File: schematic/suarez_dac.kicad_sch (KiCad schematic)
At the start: 26 parts, among them M1 1 / 0.15 um, M10 2 / 0.35 um LVT, M11 1 / 0.15 um, M12 2 / 0.35 um LVT, M13 4 / 2 um, M14 4 / 2 um, M15 4 / 1 um LVT, M16 4 / 1 um LVT, M17 4 / 2 um, M18 4 / 2 um, M19 24 / 2 um, M2 2 / 0.15 um, M20 20 / 1 um, M3 1 / 0.15 um, M4 2 / 0.15 um, M5 1 / 0.15 um, M6 2 / 0.15 um, M7 1 / 0.15 um, M8 2 / 0.35 um LVT, M9 1 / 0.15 um

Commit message: Connect schematic signal path and add illustrated design documentation
Draw reference selection, SAMPLE/HOLD banks, amplifier bias, feedback,
output stage, and compensation as connected circuits. Retain device pin
numbers, models, geometry, and the qualified silicon implementation.

Add schematic, actual-GDS, all-code, mismatch, stability, settling, and
phase-timing figures, plus circuit, testing, and reproduction guides.

Validation: zero KiCad ERC violations; 72 pin connections, all 26 device
property sets, and symbol pin names match design.json. All 87 local
documentation links resolve; evidence audit passes. GDS and RC hashes
remain unchanged. Refresh the release manifest and figure generators.
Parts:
- removed M10, M12, M8: 2 / 0.35 um LVT, symbol Sky130:PMOS_TG3
- removed M11, M7, M9: 1 / 0.15 um, symbol Sky130:NMOS3
- removed M16: 4 / 1 um LVT, symbol Sky130:PMOS3
- removed M17: 4 / 2 um, symbol Sky130:NMOS3
- removed R1, R2: 171 kR nominal, symbol Sky130:R_Small_US
- added M10, M12, M8: 2 / 0.35 um LVT, symbol Sky130:PMOS_H3
- added M11, M7, M9: 1 / 0.15 um, symbol Sky130:NMOS_H3
- added M16: 4 / 1 um LVT, symbol Sky130:PMOS_R3
- added M17: 4 / 2 um, symbol Sky130:NMOS_R3
- added R1, R2: 171 kR, symbol Sky130:R_Small_US_H
- R3: value 80 kR nominal -> 80 kR
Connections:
- net BIAS: now also R1.1
- net HOLD: now also M11.3 (S), M12.3 (S)
- net H_BAR: now also M8.2 (G)
- net L_BAR: now also M10.2 (G)
- net MIRROR: now also M16.1 (D), M17.1 (D), M17.2 (G)
- net RBMID: now also R1.2, R2.1
- net SAMPLE: now also M10.3 (S), M11.1 (D), M12.1 (D), M7.3 (S), M8.3 (S), M9.3 (S)
- net S_BAR: now also M12.2 (G)
- net TAIL: now also M16.3 (S)
- net VGND: now also M17.3 (S), R2.2
- net ua[0]: now also M7.1 (D), M8.1 (D)
- net ua[1]: now also M16.2 (G)
- net ua[2]: now also M10.1 (D), M9.1 (D)
- net ui_in[0]: now also M7.2 (G)
- net ui_in[1]: now also M9.2 (G)
- net ui_in[2]: now also M11.2 (G)
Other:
- note added: "01 REFERENCE SELECTION AND CHARGE SHARING"
- note added: "02 UNITY-GAIN BUFFER / BIAS, FEEDBACK AND COMPENSATION"
- note added: "03 COMPLEMENTARY PHASE DRIVERS"
- note added: "8 bits, LSB first: charge 2 us; dead 0.2 us; share 2 us; dead 0.2 us. Read 3 us after bit 7."
- note added: "Bodies: all NMOS -> VGND; all PMOS -> VDPWR. Body ties are explicit in SPICE / silicon."
- note added: "C1 / C2: 16 MIM units per bank"
- note added: "HIGH"
- note added: "HIGH / LOW never overlap. LOW / SHARE overlap only during initialization. External controller supplies dead time."
- note added: "Initialize: HIGH=0, LOW=1, SHARE=1 for 8 us. Then all phases off for 0.2 us."
- note added: "LOW"
- note added: "OPERATING SEQUENCE"
- note added: "R3-C3 compensation belongs to the buffer"
- note added: "SHARE"
- note added: "SKY130 | 1.8 V | 8 bits, LSB first | 161 x 225.76 um | W / L dimensions in um"
- note added: "SUAREZ SERIAL CHARGE-SHARING DAC"
- note added: "Switches: N 1 / 0.15; P 2 / 0.35 LVT"
- note added: "VOUT"
- note added: "VREFH = 0.9 V"
- note added: "VREFL = 0.2 V"
- note added: "unity-gain feedback"
- note removed: "01 CHARGE REDISTRIBUTION"
- note removed: "02 BUFFER COMPENSATION"
- note removed: "03 COMPLEMENTARY SWITCH CONTROLS"
- note removed: "04 INPUT AMPLIFIER AND BIAS"
- note removed: "05 OUTPUT DRIVER"
- note removed: "16 x (14 / 14 um) MIM"
- note removed: "Buffered analog output"
- note removed: "Bulk ties: every NMOS -> VGND; every PMOS -> VDPWR. Bulk pins are implicit in this drawing and explicit in the silicon netlist."
- note removed: "C1 and C2 perform the D/A conversion."
- note removed: "C3 stabilizes the output buffer."
- note removed: "CHARGE HIGH"
- note removed: "CHARGE LOW"
- note removed: "External phases provide dead time."
- note removed: "HIGH and LOW must never overlap. SHARE closes only after HIGH / LOW have opened."
- note removed: "Initialize: HIGH=0, LOW=1, SHARE=1 for 8 us. Then 8 bits, LSB first: charge 2 us, dead 0.2 us, share 2 us, dead 0.2 us."
- note removed: "No on-chip word counter is required."
- note removed: "PORTS"
- note removed: "R3: xhigh poly, 0.35 / 14 um"
- note removed: "SHARE CHARGE"
- note removed: "SUAREZ TWO-CAPACITOR DAC / SKY130"
- note removed: "Tiny Tapeout 1x2 analog macro | 1.8 V | LSB first | transistor dimensions shown as W / L"
- note removed: "Unused digital outputs are tied to VGND; ua[3:7] are isolated. Supply bypassing is provided by the Tiny Tapeout chip / board."
- note removed: "ui_in[0] = HIGH ui_in[1] = LOW ui_in[2] = SHARE ua[0] = VREFH ua[1] = VOUT ua[2] = VREFL"
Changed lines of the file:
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@@
 (kicad_sch (version 20250114) (generator "eeschema")
-(paper "A3") (title_block (title "Suarez two-capacitor DAC") (rev "0.1") (company "SKY130 / Tiny Tapeout"))
+(paper "A3") (title_block (title "Suarez two-capacitor DAC") (rev "0.2") (company "SKY130 / Tiny Tapeout"))

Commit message: Clean up ground symbols and shared supply rails
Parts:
- removed R1, R2: 171 kR, symbol Sky130:R_Small_US_H
- added R1, R2: 171 kR, symbol Sky130:R_Small_US
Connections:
- net BIAS: now also R1.1
- net RBMID: now also R1.2, R2.1
- net VGND: now also R2.2
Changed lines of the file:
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@@
 (kicad_sch (version 20250114) (generator "eeschema")
-(paper "A3") (title_block (title "Suarez two-capacitor DAC") (rev "0.2") (company "SKY130 / Tiny Tapeout"))
+(paper "A3") (title_block (title "Suarez two-capacitor DAC") (rev "0.3") (company "SKY130 / Tiny Tapeout"))

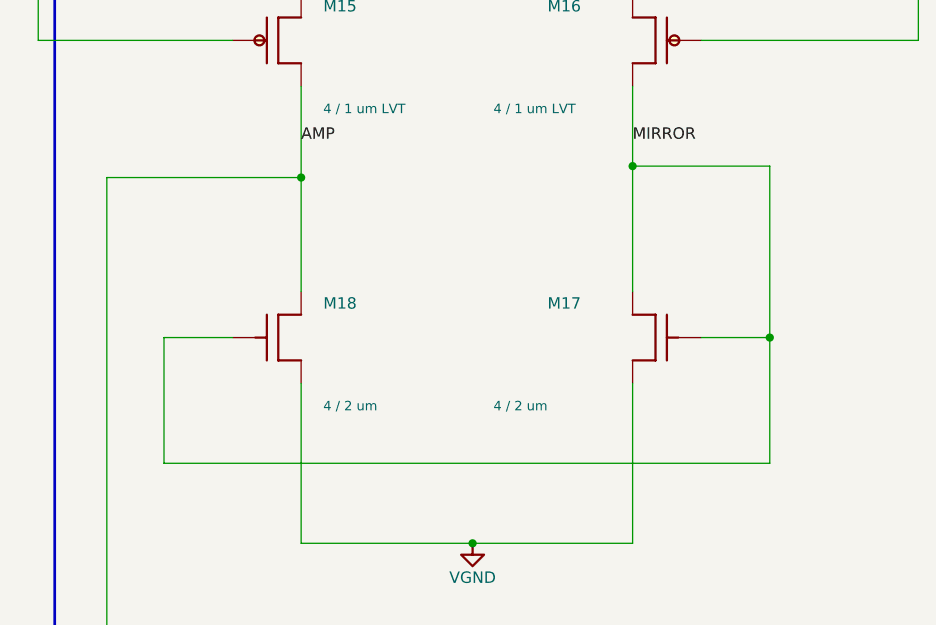
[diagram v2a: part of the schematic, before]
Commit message: Redraw buffer current mirror in conventional schematic form
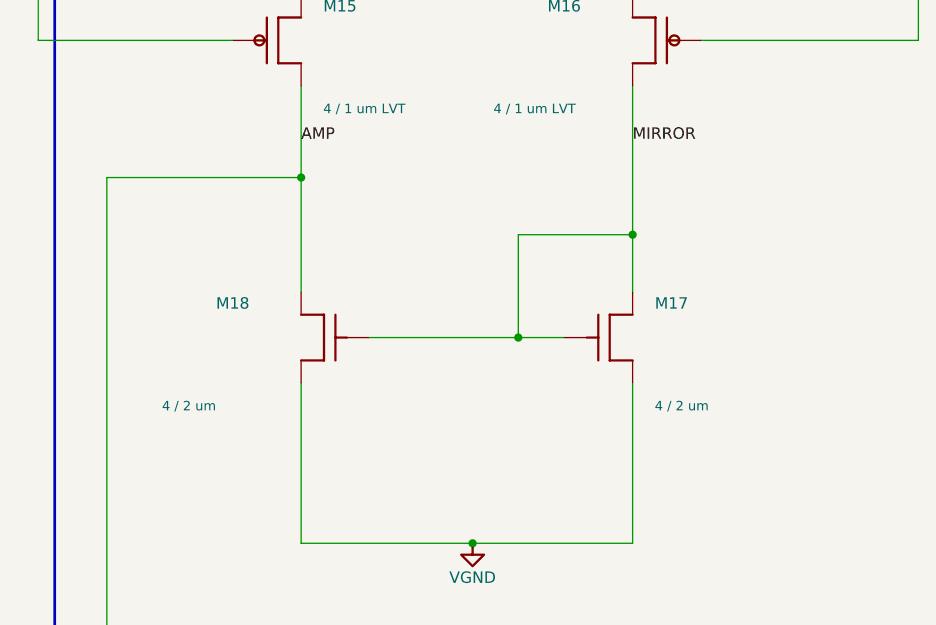
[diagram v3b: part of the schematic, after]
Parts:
- removed M17: 4 / 2 um, symbol Sky130:NMOS_R3
- removed M18: 4 / 2 um, symbol Sky130:NMOS3
- added M17: 4 / 2 um, symbol Sky130:NMOS3
- added M18: 4 / 2 um, symbol Sky130:NMOS_R3
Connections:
- net AMP: now also M18.1 (D)
- net MIRROR: now also M17.1 (D), M17.2 (G), M18.2 (G)
- net VGND: now also M17.3 (S), M18.3 (S)
